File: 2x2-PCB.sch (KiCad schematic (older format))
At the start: 24 parts, among them SW1 SW_Push, U1 ATmega32U4-AU, Y1 16MHz

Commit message: placed all components on board
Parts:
- U1: footprint Package_QFP:TQFP-44_10x10mm_P0.8mm -> Housings_QFP:TQFP-44_10x10mm_Pitch0.8mm
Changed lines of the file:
@@
 F 0 "U1" H 4560 2151 50  0000 C CNN
 F 1 "ATmega32U4-AU" H 4560 2060 50  0000 C CNN
-F 2 "Package_QFP:TQFP-44_10x10mm_P0.8mm" H 4560 4040 50  0001 C CIN
+F 2 "Housings_QFP:TQFP-44_10x10mm_Pitch0.8mm" H 4560 4040 50  0001 C CIN
 F 3 "http://ww1.microchip.com/downloads/en/DeviceDoc/Atmel-7766-8-bit-AVR-ATmega16U4-32U4_Datasheet.pdf" H 4560 4040 50  0001 C CNN
 	1    4560 4040

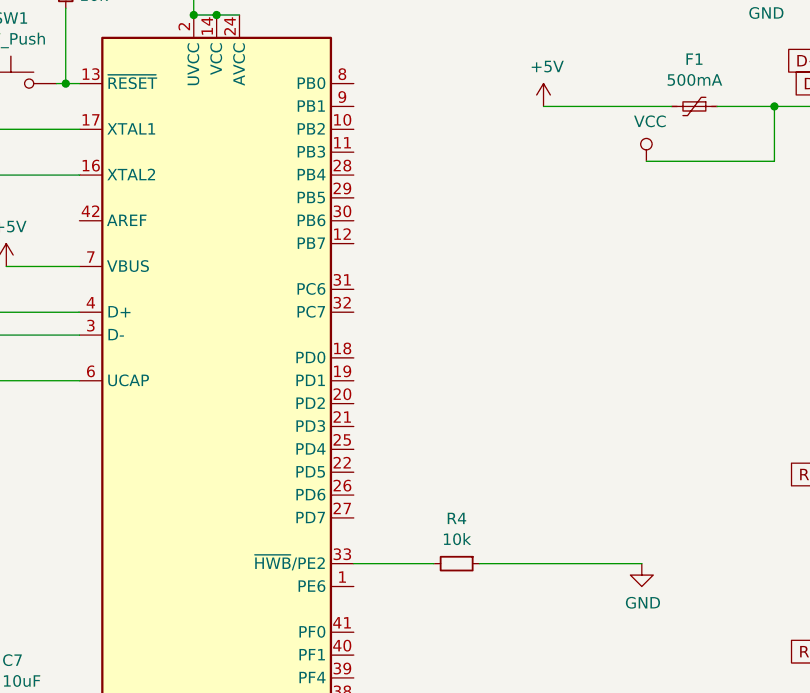
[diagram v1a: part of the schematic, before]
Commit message: added tracks and traces
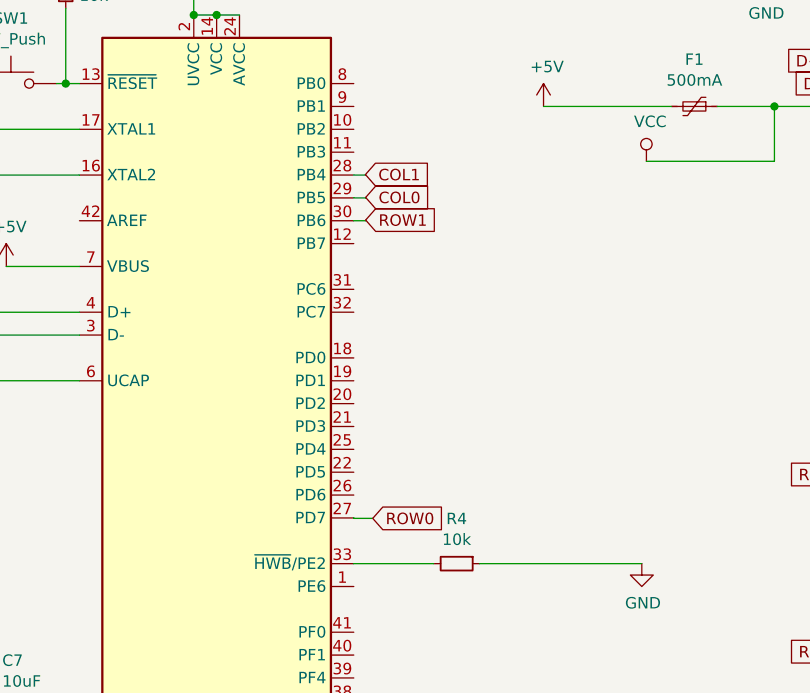
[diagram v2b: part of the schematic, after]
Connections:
- wire segments 71 -> 79
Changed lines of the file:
@@
 Text GLabel 7375 5025 0    50   Input ~ 0
 ROW1
+Text GLabel 5243 4442 2    50   Input ~ 0
+ROW0
+Wire Wire Line
+	5243 4442 5160 4442
+Wire Wire Line
+	5160 4442 5160 4440
+Text GLabel 5211 2938 2    50   Input ~ 0
+COL1
+Text GLabel 5212 3137 2    50   Input ~ 0
+ROW1
+Text GLabel 5212 3038 2    50   Input ~ 0
+COL0
+Wire Wire Line
+	5160 2940 5211 2940
+Wire Wire Line
+	5211 2940 5211 2938
+Wire Wire Line
+	5160 3040 5212 3040
+Wire Wire Line
+	5212 3040 5212 3038
+Wire Wire Line
+	5160 3140 5212 3140
+Wire Wire Line
+	5212 3140 5212 3137
 $EndSCHEMATC
